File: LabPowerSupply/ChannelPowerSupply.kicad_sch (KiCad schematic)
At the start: 0 parts

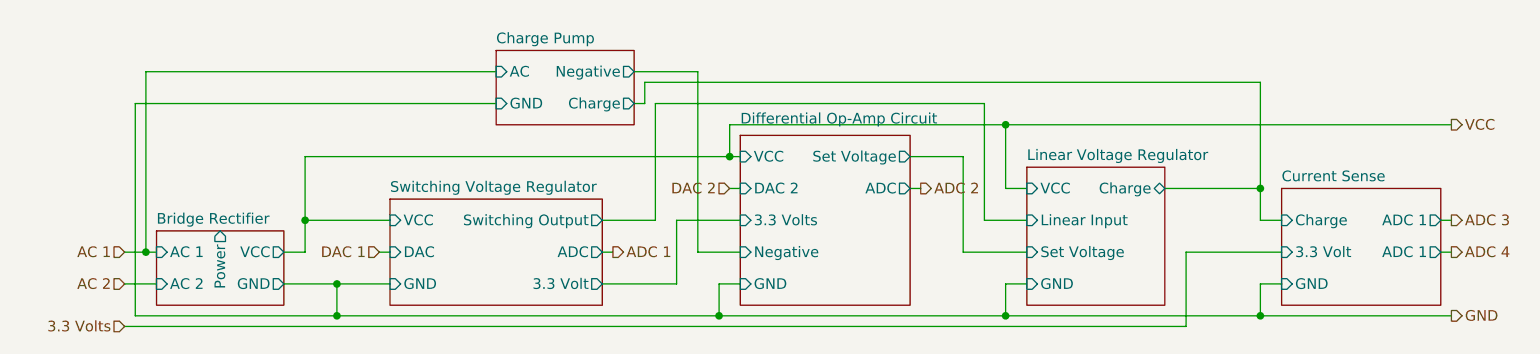
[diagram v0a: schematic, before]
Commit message: Finished first pass on the schematic
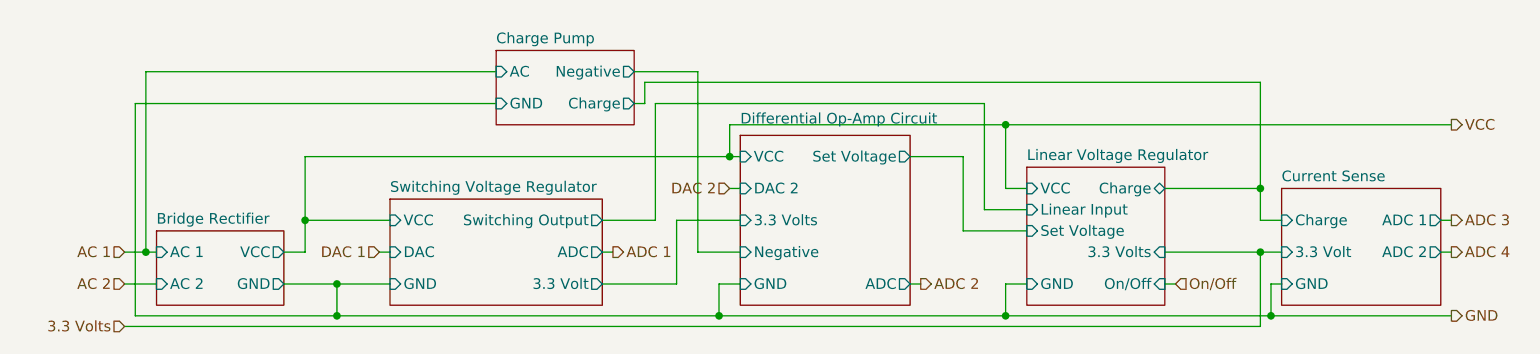
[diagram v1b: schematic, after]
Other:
- sheet Bridge Rectifier ports: added none; removed Power
- sheet Current Sense  ports: added ADC 2; removed none
- sheet Linear Voltage Regulator  ports: added 3.3 Volts, On/Off; removed none
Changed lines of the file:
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@@
   (junction (at 143.51 90.17) (diameter 0) (color 0 0 0 0)
   )
-  (junction (at 207.01 109.22) (diameter 0) (color 0 0 0 0)
-  )
   (junction (at 92.71 97.79) (diameter 0) (color 0 0 0 0)
   )
@@
   (junction (at 96.52 109.22) (diameter 0) (color 0 0 0 0)
   )
+  (junction (at 208.28 109.22) (diameter 0) (color 0 0 0 0)
+  )
+  (junction (at 207.01 101.6) (diameter 0) (color 0 0 0 0)
+  )
   (junction (at 207.01 93.98) (diameter 0) (color 0 0 0 0)
   )
@@
     (stroke (width 0) (type default) (color 0 0 0 0))
   )
-  (wire (pts (xy 207.01 109.22) (xy 229.87 109.22))
-    (stroke (width 0) (type default) (color 0 0 0 0))
-  )
   (wire (pts (xy 142.24 109.22) (xy 176.53 109.22))
     (stroke (width 0) (type default) (color 0 0 0 0))
   )
+  (wire (pts (xy 176.53 109.22) (xy 208.28 109.22))
+    (stroke (width 0) (type default) (color 0 0 0 0))
+  )
   (wire (pts (xy 90.17 105.41) (xy 96.52 105.41))
     (stroke (width 0) (type default) (color 0 0 0 0))
@@
     (stroke (width 0) (type default) (color 0 0 0 0))
   )
-  (wire (pts (xy 207.01 105.41) (xy 209.55 105.41))
+  (wire (pts (xy 208.28 105.41) (xy 209.55 105.41))
     (stroke (width 0) (type default) (color 0 0 0 0))
   )
@@
     (stroke (width 0) (type default) (color 0 0 0 0))
   )
-  (wire (pts (xy 171.45 90.17) (xy 171.45 101.6))
+  (wire (pts (xy 195.58 101.6) (xy 207.01 101.6))
+    (stroke (width 0) (type default) (color 0 0 0 0))
+  )
+  (wire (pts (xy 171.45 90.17) (xy 171.45 99.06))
     (stroke (width 0) (type default) (color 0 0 0 0))
   )
@@
     (stroke (width 0) (type default) (color 0 0 0 0))
   )
-  (wire (pts (xy 209.55 101.6) (xy 198.12 101.6))
+  (wire (pts (xy 209.55 101.6) (xy 207.01 101.6))
     (stroke (width 0) (type default) (color 0 0 0 0))
   )
@@
     (stroke (width 0) (type default) (color 0 0 0 0))
   )
-  (wire (pts (xy 171.45 101.6) (xy 179.07 101.6))
+  (wire (pts (xy 171.45 99.06) (xy 179.07 99.06))
     (stroke (width 0) (type default) (color 0 0 0 0))
   )
@@
     (stroke (width 0) (type default) (color 0 0 0 0))
   )
+  (wire (pts (xy 208.28 109.22) (xy 229.87 109.22))
+    (stroke (width 0) (type default) (color 0 0 0 0))
+  )
   (wire (pts (xy 165.1 90.17) (xy 171.45 90.17))
     (stroke (width 0) (type default) (color 0 0 0 0))
@@
     (stroke (width 0) (type default) (color 0 0 0 0))
   )
-  (wire (pts (xy 165.1 93.98) (xy 166.37 93.98))
+  (wire (pts (xy 165.1 105.41) (xy 166.37 105.41))
     (stroke (width 0) (type default) (color 0 0 0 0))
   )
@@
     (stroke (width 0) (type default) (color 0 0 0 0))
   )
-  (wire (pts (xy 198.12 101.6) (xy 198.12 110.49))
+  (wire (pts (xy 207.01 101.6) (xy 207.01 110.49))
     (stroke (width 0) (type default) (color 0 0 0 0))
   )
@@
     (stroke (width 0) (type default) (color 0 0 0 0))
   )
-  (wire (pts (xy 71.12 110.49) (xy 198.12 110.49))
-    (stroke (width 0) (type default) (color 0 0 0 0))
-  )
-  (wire (pts (xy 176.53 109.22) (xy 207.01 109.22))
+  (wire (pts (xy 71.12 110.49) (xy 207.01 110.49))
     (stroke (width 0) (type default) (color 0 0 0 0))
   )
@@
     (stroke (width 0) (type default) (color 0 0 0 0))
   )
-  (wire (pts (xy 207.01 105.41) (xy 207.01 109.22))
+  (wire (pts (xy 208.28 105.41) (xy 208.28 109.22))
     (stroke (width 0) (type default) (color 0 0 0 0))
   )
@@
     (stroke (width 0) (type default) (color 0 0 0 0))
   )
+  (wire (pts (xy 195.58 105.41) (xy 196.85 105.41))
+    (stroke (width 0) (type default) (color 0 0 0 0))
+  )
   (wire (pts (xy 207.01 93.98) (xy 207.01 97.79))
     (stroke (width 0) (type default) (color 0 0 0 0))
   )
-  (wire (pts (xy 179.07 97.79) (xy 173.99 97.79))
+  (wire (pts (xy 179.07 96.52) (xy 173.99 96.52))
     (stroke (width 0) (type default) (color 0 0 0 0))
   )
@@
     (stroke (width 0) (type default) (color 0 0 0 0))
   )
-  (wire (pts (xy 173.99 97.79) (xy 173.99 83.82))
+  (wire (pts (xy 173.99 96.52) (xy 173.99 83.82))
     (stroke (width 0) (type default) (color 0 0 0 0))
   )
@@
     (effects (font (size 1.27 1.27)) (justify left))
   )
+  (hierarchical_label "On{slash}Off" (shape input) (at 196.85 105.41 0)
+    (effects (font (size 1.27 1.27)) (justify left))
+  )
+  (hierarchical_label "ADC 2" (shape output) (at 166.37 105.41 0)
+    (effects (font (size 1.27 1.27)) (justify left))
+  )
   (hierarchical_label "AC 2" (shape input) (at 71.12 105.41 180)
     (effects (font (size 1.27 1.27)) (justify right))
@@
     (effects (font (size 1.27 1.27)) (justify left))
   )
-  (hierarchical_label "ADC 2" (shape output) (at 166.37 93.98 0)
-    (effects (font (size 1.27 1.27)) (justify left))
-  )
   (hierarchical_label "3.3 Volts" (shape input) (at 71.12 110.49 180)
     (effects (font (size 1.27 1.27)) (justify right))
@@
       (effects (font (size 1.27 1.27)) (justify left top) hide)
     )
-    (pin "Set Voltage" input (at 179.07 101.6 180)
+    (pin "Set Voltage" input (at 179.07 99.06 180)
       (effects (font (size 1.27 1.27)) (justify left))
     )
@@
       (effects (font (size 1.27 1.27)) (justify right))
     )
-    (pin "Linear Input" input (at 179.07 97.79 180)
+    (pin "Linear Input" input (at 179.07 96.52 180)
       (effects (font (size 1.27 1.27)) (justify left))
     )
@@
       (effects (font (size 1.27 1.27)) (justify left))
     )
+    (pin "On{slash}Off" input (at 195.58 105.41 0)
+      (effects (font (size 1.27 1.27)) (justify right))
+    )
+    (pin "3.3 Volts" input (at 195.58 101.6 0)
+      (effects (font (size 1.27 1.27)) (justify right))
+    )
   )
   (sheet (at 102.87 95.25) (size 25.4 12.7) (fields_autoplaced)
@@
       (effects (font (size 1.27 1.27)) (justify left))
     )
-    (pin "ADC" output (at 165.1 93.98 0)
+    (pin "ADC" output (at 165.1 105.41 0)
       (effects (font (size 1.27 1.27)) (justify right))
     )
@@
       (effects (font (size 1.27 1.27)) (justify left top) hide)
     )
-    (pin "ADC 1" output (at 228.6 101.6 0)
-      (effects (font (size 1.27 1.27)) (justify right))
-    )
     (pin "Charge" input (at 209.55 97.79 180)
       (effects (font (size 1.27 1.27)) (justify left))
@@
       (effects (font (size 1.27 1.27)) (justify right))
     )
+    (pin "ADC 2" output (at 228.6 101.6 0)
+      (effects (font (size 1.27 1.27)) (justify right))
+    )
   )
   (sheet (at 74.93 99.06) (size 15.24 8.89) (fields_autoplaced)
@@
       (effects (font (size 1.27 1.27)) (justify right))
     )
-    (pin "Power" output (at 82.55 99.06 90)
-      (effects (font (size 1.27 1.27)) (justify right))
-    )

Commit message: more work
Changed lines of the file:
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@@
       (effects (font (size 1.27 1.27)) (justify left))
     )
-    (pin "Charge" bidirectional (at 195.58 88.9 0)
+    (pin "Charge" output (at 195.58 88.9 0)
       (effects (font (size 1.27 1.27)) (justify right))
     )

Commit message: almost done
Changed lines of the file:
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@@
     (rev "1")
     (company "George Mason University")
+    (comment 1 "digitally controlled by its microcontroller.")
+    (comment 2 "the user-requested voltage at the banana plugs. This circuit is")
+    (comment 3 "supply. This circuit converts the 12Vrms from the transformer into")
+    (comment 4 "This is the layout for the analog power electronics for the power")
   )
   (junction (at 143.51 90.17) (diameter 0) (color 0 0 0 0)
@@
   (junction (at 96.52 105.41) (diameter 0) (color 0 0 0 0)
   )
+  (junction (at 73.66 101.6) (diameter 0) (color 0 0 0 0)
+  )
+  (junction (at 96.52 109.22) (diameter 0) (color 0 0 0 0)
+  )
+  (junction (at 208.28 109.22) (diameter 0) (color 0 0 0 0)
+  )
   (junction (at 207.01 88.9) (diameter 0) (color 0 0 0 0)
   )
-  (junction (at 73.66 101.6) (diameter 0) (color 0 0 0 0)
-  )
-  (junction (at 96.52 109.22) (diameter 0) (color 0 0 0 0)
-  )
-  (junction (at 177.8 109.22) (diameter 0) (color 0 0 0 0)
-  )
-  (junction (at 208.28 109.22) (diameter 0) (color 0 0 0 0)
+  (junction (at 199.39 109.22) (diameter 0) (color 0 0 0 0)
   )
   (wire (pts (xy 207.01 97.79) (xy 209.55 97.79))
@@
     (stroke (width 0) (type default) (color 0 0 0 0))
   )
-  (wire (pts (xy 176.53 102.87) (xy 176.53 110.49))
+  (wire (pts (xy 176.53 104.14) (xy 176.53 110.49))
     (stroke (width 0) (type default) (color 0 0 0 0))
   )
@@
     (stroke (width 0) (type default) (color 0 0 0 0))
   )
+  (wire (pts (xy 199.39 104.14) (xy 199.39 109.22))
+    (stroke (width 0) (type default) (color 0 0 0 0))
+  )
+  (wire (pts (xy 139.7 78.74) (xy 139.7 101.6))
+    (stroke (width 0) (type default) (color 0 0 0 0))
+  )
+  (wire (pts (xy 128.27 105.41) (xy 138.43 105.41))
+    (stroke (width 0) (type default) (color 0 0 0 0))
+  )
+  (wire (pts (xy 96.52 109.22) (xy 143.51 109.22))
+    (stroke (width 0) (type default) (color 0 0 0 0))
+  )
+  (wire (pts (xy 196.85 104.14) (xy 199.39 104.14))
+    (stroke (width 0) (type default) (color 0 0 0 0))
+  )
+  (wire (pts (xy 132.08 78.74) (xy 139.7 78.74))
+    (stroke (width 0) (type default) (color 0 0 0 0))
+  )
+  (wire (pts (xy 176.53 110.49) (xy 207.01 110.49))
+    (stroke (width 0) (type default) (color 0 0 0 0))
+  )
+  (wire (pts (xy 165.1 105.41) (xy 166.37 105.41))
+    (stroke (width 0) (type default) (color 0 0 0 0))
+  )
+  (wire (pts (xy 177.8 78.74) (xy 229.87 78.74))
+    (stroke (width 0) (type default) (color 0 0 0 0))
+  )
+  (wire (pts (xy 71.12 105.41) (xy 74.93 105.41))
+    (stroke (width 0) (type default) (color 0 0 0 0))
+  )
+  (wire (pts (xy 207.01 101.6) (xy 207.01 110.49))
+    (stroke (width 0) (type default) (color 0 0 0 0))
+  )
   (wire (pts (xy 207.01 88.9) (xy 207.01 97.79))
     (stroke (width 0) (type default) (color 0 0 0 0))
   )
-  (wire (pts (xy 139.7 78.74) (xy 139.7 101.6))
-    (stroke (width 0) (type default) (color 0 0 0 0))
-  )
-  (wire (pts (xy 177.8 109.22) (xy 208.28 109.22))
-    (stroke (width 0) (type default) (color 0 0 0 0))
-  )
-  (wire (pts (xy 128.27 105.41) (xy 138.43 105.41))
-    (stroke (width 0) (type default) (color 0 0 0 0))
-  )
-  (wire (pts (xy 96.52 109.22) (xy 143.51 109.22))
-    (stroke (width 0) (type default) (color 0 0 0 0))
-  )
-  (wire (pts (xy 132.08 78.74) (xy 139.7 78.74))
-    (stroke (width 0) (type default) (color 0 0 0 0))
-  )
-  (wire (pts (xy 176.53 110.49) (xy 207.01 110.49))
-    (stroke (width 0) (type default) (color 0 0 0 0))
-  )
-  (wire (pts (xy 165.1 105.41) (xy 166.37 105.41))
-    (stroke (width 0) (type default) (color 0 0 0 0))
-  )
-  (wire (pts (xy 177.8 105.41) (xy 179.07 105.41))
-    (stroke (width 0) (type default) (color 0 0 0 0))
-  )
-  (wire (pts (xy 177.8 78.74) (xy 229.87 78.74))
-    (stroke (width 0) (type default) (color 0 0 0 0))
-  )
-  (wire (pts (xy 71.12 105.41) (xy 74.93 105.41))
-    (stroke (width 0) (type default) (color 0 0 0 0))
-  )
-  (wire (pts (xy 207.01 101.6) (xy 207.01 110.49))
+  (wire (pts (xy 199.39 109.22) (xy 208.28 109.22))
     (stroke (width 0) (type default) (color 0 0 0 0))
   )
@@
     (stroke (width 0) (type default) (color 0 0 0 0))
   )
-  (wire (pts (xy 177.8 105.41) (xy 177.8 109.22))
-    (stroke (width 0) (type default) (color 0 0 0 0))
-  )
   (wire (pts (xy 228.6 97.79) (xy 229.87 97.79))
     (stroke (width 0) (type default) (color 0 0 0 0))
@@
     (stroke (width 0) (type default) (color 0 0 0 0))
   )
-  (wire (pts (xy 143.51 109.22) (xy 177.8 109.22))
+  (wire (pts (xy 196.85 88.9) (xy 207.01 88.9))
+    (stroke (width 0) (type default) (color 0 0 0 0))
+  )
+  (wire (pts (xy 143.51 109.22) (xy 199.39 109.22))
     (stroke (width 0) (type default) (color 0 0 0 0))
   )
@@
     (stroke (width 0) (type default) (color 0 0 0 0))
   )
-  (wire (pts (xy 179.07 102.87) (xy 176.53 102.87))
+  (wire (pts (xy 179.07 104.14) (xy 176.53 104.14))
     (stroke (width 0) (type default) (color 0 0 0 0))
   )
@@
     (stroke (width 0) (type default) (color 0 0 0 0))
   )
-  (wire (pts (xy 195.58 88.9) (xy 207.01 88.9))
-    (stroke (width 0) (type default) (color 0 0 0 0))
-  )
   (hierarchical_label "DAC 2" (shape input) (at 143.51 93.98 180)
     (effects (font (size 1.27 1.27)) (justify right))
@@
     (effects (font (size 1.27 1.27)) (justify right))
   )
-  (sheet (at 179.07 86.36) (size 16.51 21.59) (fields_autoplaced)
+  (sheet (at 179.07 86.36) (size 17.78 21.59) (fields_autoplaced)
     (stroke (width 0.1524) (type solid) (color 0 0 0 0))
     (fill (color 0 0 0 0.0000))
@@
       (effects (font (size 1.27 1.27)) (justify left))
     )
-    (pin "Charge" output (at 195.58 88.9 0)
+    (pin "Charge" output (at 196.85 88.9 0)
       (effects (font (size 1.27 1.27)) (justify right))
     )
@@
       (effects (font (size 1.27 1.27)) (justify left))
     )
-    (pin "GND" input (at 179.07 105.41 180)
-      (effects (font (size 1.27 1.27)) (justify left))
+    (pin "GND" input (at 196.85 104.14 0)
+      (effects (font (size 1.27 1.27)) (justify right))
     )
     (pin "On{slash}Off" input (at 179.07 100.33 180)
       (effects (font (size 1.27 1.27)) (justify left))
     )
-    (pin "3.3 Volts" input (at 179.07 102.87 180)
-      (effects (font (size 1.27 1.27)) (justify left))
-    )
+    (pin "3.3 Volts" input (at 179.07 104.14 180)
+      (effects (font (size 1.27 1.27)) (justify left))
+    )

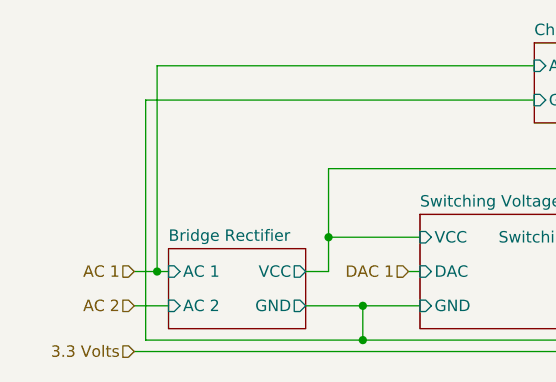
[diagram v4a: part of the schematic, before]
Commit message: Moved charge pump
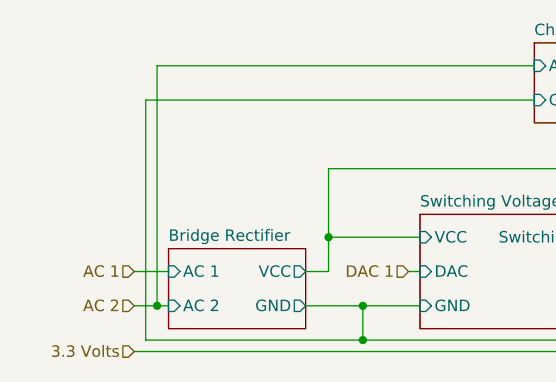
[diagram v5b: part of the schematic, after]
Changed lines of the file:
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@@
   (junction (at 96.52 105.41) (diameter 0) (color 0 0 0 0)
-  )
-  (junction (at 73.66 101.6) (diameter 0) (color 0 0 0 0)
   )
   (junction (at 96.52 109.22) (diameter 0) (color 0 0 0 0)
@@
   (junction (at 207.01 88.9) (diameter 0) (color 0 0 0 0)
   )
+  (junction (at 73.66 105.41) (diameter 0) (color 0 0 0 0)
+  )
   (junction (at 199.39 109.22) (diameter 0) (color 0 0 0 0)
   )
@@
     (stroke (width 0) (type default) (color 0 0 0 0))
   )
-  (wire (pts (xy 73.66 101.6) (xy 73.66 78.74))
+  (wire (pts (xy 73.66 78.74) (xy 73.66 105.41))
     (stroke (width 0) (type default) (color 0 0 0 0))
   )
@@
   )
   (wire (pts (xy 134.62 83.82) (xy 134.62 97.79))
-    (stroke (width 0) (type default) (color 0 0 0 0))
-  )
-  (wire (pts (xy 73.66 101.6) (xy 74.93 101.6))
     (stroke (width 0) (type default) (color 0 0 0 0))
   )
@@
     (stroke (width 0) (type default) (color 0 0 0 0))
   )
-  (wire (pts (xy 71.12 105.41) (xy 74.93 105.41))
+  (wire (pts (xy 71.12 105.41) (xy 73.66 105.41))
     (stroke (width 0) (type default) (color 0 0 0 0))
   )
@@
     (stroke (width 0) (type default) (color 0 0 0 0))
   )
+  (wire (pts (xy 73.66 105.41) (xy 74.93 105.41))
+    (stroke (width 0) (type default) (color 0 0 0 0))
+  )
   (wire (pts (xy 179.07 104.14) (xy 176.53 104.14))
     (stroke (width 0) (type default) (color 0 0 0 0))
@@
     (stroke (width 0) (type default) (color 0 0 0 0))
   )
-  (wire (pts (xy 71.12 101.6) (xy 73.66 101.6))
+  (wire (pts (xy 71.12 101.6) (xy 74.93 101.6))
     (stroke (width 0) (type default) (color 0 0 0 0))
   )
